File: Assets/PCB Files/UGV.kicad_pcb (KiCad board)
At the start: 2 copper layers, 120.6 x 156.5 mm, 78 parts, among them J13 USB3_A, J15 Screw_Terminal_01x12, J16 Screw_Terminal_01x12, J17 Screw_Terminal_01x12, J18 Screw_Terminal_01x12, Q1 AO3400A, U2 LMR33630ADDA, U3 SN74LVC8T245, U4 Teensy4.1, U5 SN74LVC8T245

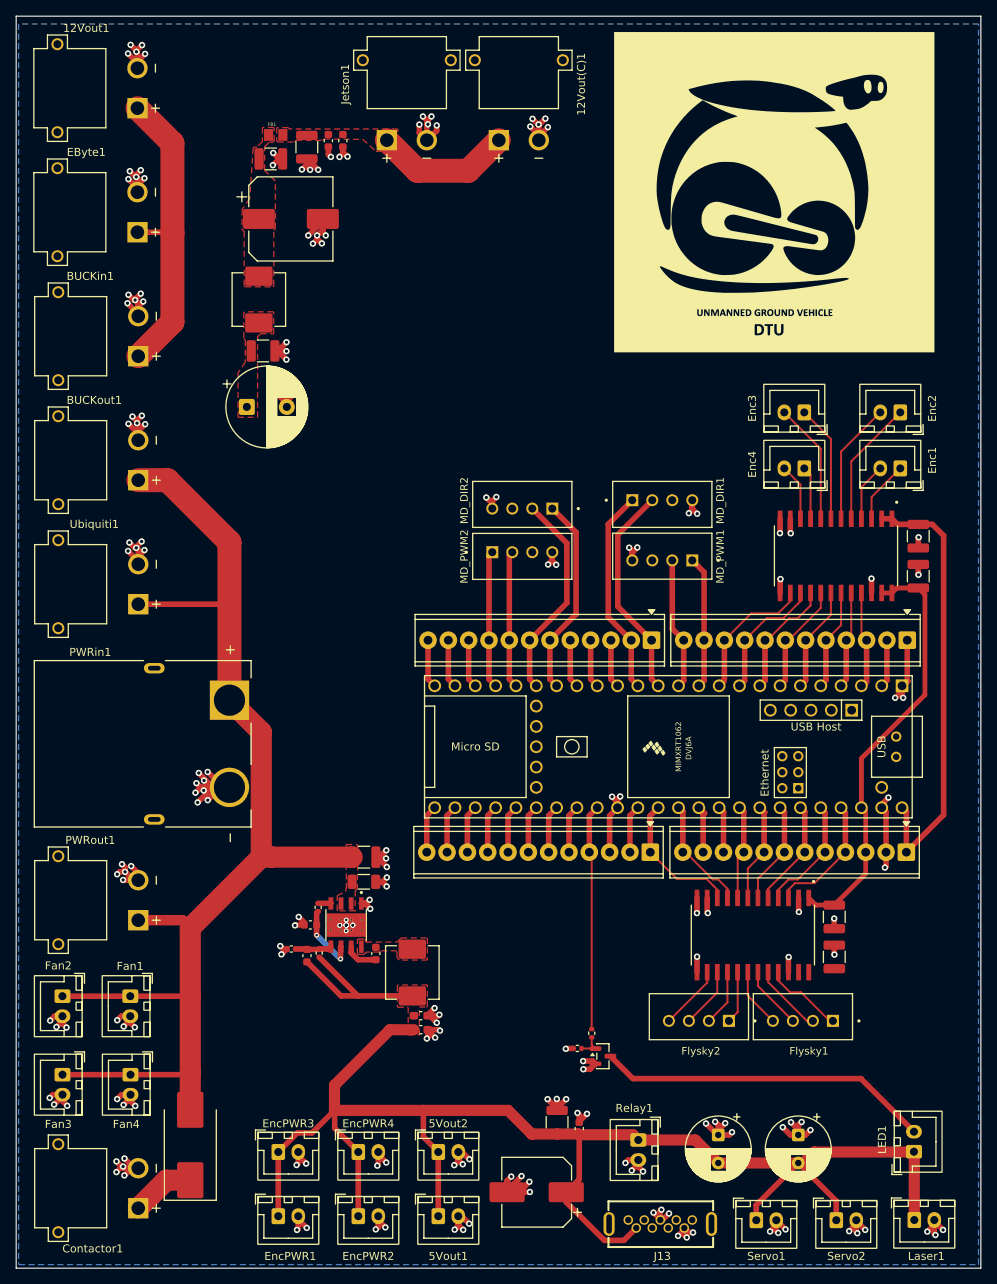
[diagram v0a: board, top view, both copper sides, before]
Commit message: Changed the footprint
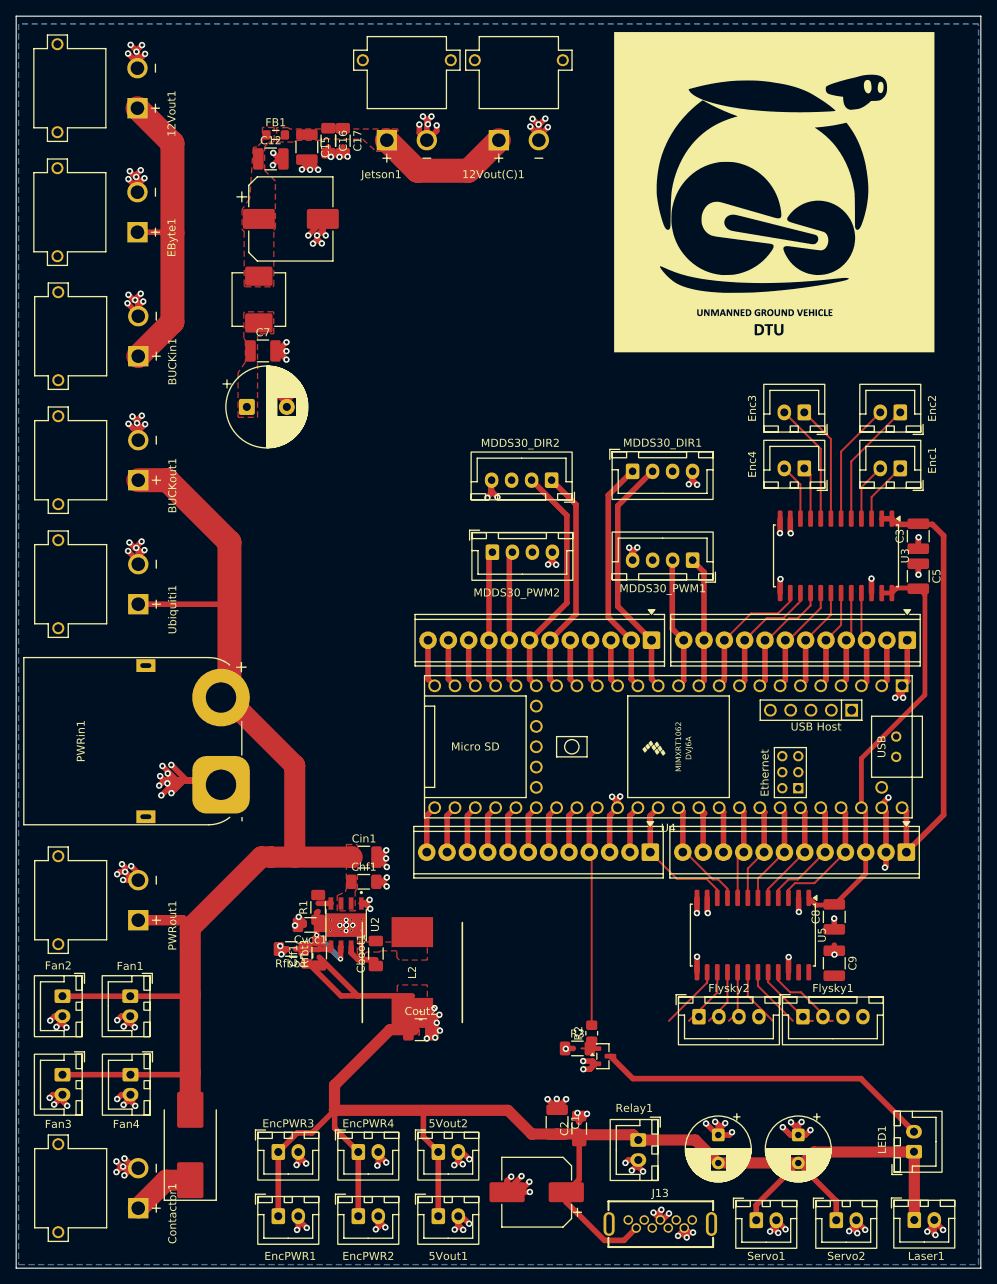
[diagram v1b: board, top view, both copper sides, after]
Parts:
- removed MD_DIR1, MD_DIR2, MD_PWM1, MD_PWM2: B4B-XH-A_LF__SN_, B4B-XH-A_LF__SN_:JST_B4B-XH-A_LF__SN_
- added MDDS30_DIR1: B4B-XH-A_LF__SN_, Connector_JST:JST_XH_B4B-XH-A_1x04_P2.50mm_Vertical, F.Cu at (77.8, 57.9)
- added MDDS30_DIR2: B4B-XH-A_LF__SN_, Connector_JST:JST_XH_B4B-XH-A_1x04_P2.50mm_Vertical, F.Cu at (67.7, 59.0)
- added MDDS30_PWM1: B4B-XH-A_LF__SN_, Connector_JST:JST_XH_B4B-XH-A_1x04_P2.50mm_Vertical, F.Cu at (85.3, 69.0)
- added MDDS30_PWM2: B4B-XH-A_LF__SN_, Connector_JST:JST_XH_B4B-XH-A_1x04_P2.50mm_Vertical, F.Cu at (60.3, 68.0)
- 12Vout(C)1, 12Vout1, BUCKin1, BUCKout1, Contactor1, EByte1, Jetson1, PWRout1, Ubiquiti1: footprint XT30PW-M (1):AMASS_XT30PW-M -> UGV_Custom:AMASS_XT30PW-M
- C1, C12, C15, C3, C5, C7, C8, C9, Cin1: footprint Capacitor_SMD:C_1210_3225Metric -> Capacitor_SMD:C_1210_3225Metric_Pad1.33x2.70mm_HandSolder
- C16, C17, C2, Cboot1, Cvcc1: footprint Capacitor_SMD:C_0603_1608Metric -> Capacitor_SMD:C_1206_3216Metric_Pad1.33x1.80mm_HandSolder
- Cff1: footprint Capacitor_SMD:C_0603_1608Metric -> Capacitor_SMD:C_0805_2012Metric_Pad1.18x1.45mm_HandSolder
- Chf1: footprint Capacitor_SMD:C_1206_3216Metric -> Capacitor_SMD:C_1206_3216Metric_Pad1.33x1.80mm_HandSolder
- Cout2: footprint Capacitor_SMD:C_0603_1608Metric_Pad1.08x0.95mm_HandSolder -> Capacitor_SMD:C_1210_3225Metric_Pad1.33x2.70mm_HandSolder
- Enc1, Enc2, Enc3, Enc4: value B2B-XH-A -> B2B-XH-A-BK
- FB1: footprint BLM21PG220SN1D:BEADC2012X105N -> Inductor_SMD:L_0805_2012Metric_Pad1.05x1.20mm_HandSolder
- Fan1, Fan2, Fan3, Fan4: value B2B-XH-A -> B2B-XH-A-R
- Flysky1, Flysky2: footprint B4B-XH-A_LF__SN_:JST_B4B-XH-A_LF__SN_ -> Connector_JST:JST_XH_B4B-XH-A_1x04_P2.50mm_Vertical
- J13: footprint EasyEDA_Lib:USB-3.0-TH_U233-091N-4BLPC17-11 -> UGV_Custom:USB-3.0-TH_U233-091N-4BLPC17-11
- L2: footprint Inductor_SMD:L_Vishay_IHLP-2525 -> UGV_Custom:SRR1280-101M
- PWRin1: footprint XT90PW-M:AMASS_XT90PW-M -> Connector_AMASS:AMASS_XT90PW-M_1x02_P10.90mm_Horizontal
- R1, Rfbb1, Rfbt1: footprint Resistor_SMD:R_0402_1005Metric -> Resistor_SMD:R_1206_3216Metric_Pad1.30x1.75mm_HandSolder
- R2: footprint Resistor_SMD:R_0402_1005Metric -> Resistor_SMD:R_0805_2012Metric_Pad1.20x1.40mm_HandSolder
- R3: value 10k -> 100k; footprint Resistor_SMD:R_0402_1005Metric -> Resistor_SMD:R_1206_3216Metric_Pad1.30x1.75mm_HandSolder
- U2: footprint LMR33630ADDA:VREG_LM5017MR_NOPB -> UGV_Custom:LMR33630ADDAR
- U3, U5: footprint SN74LVC8T245DWR:SOIC127P1030X265-24N -> Package_SO:SOIC-24W_7.5x15.4mm_P1.27mm
- U4: footprint teensy.pretty-master:Teensy41 -> UGV_Custom:Teensy41
- moved PWRin1 9.79 mm to (26.3, 97.1), turned to 90 degrees
- moved C9 0.79 mm to (103.0, 119.4)
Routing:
- net /11: track 27.1 -> 30.7 mm
- net /12: track 26.0 -> 29.6 mm
- net /27: track 26.2 -> 29.8 mm
- net /26: track 25.1 -> 28.7 mm
- net Net-(D1-A): track 152.7 -> 154.5 mm
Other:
- board text added: "PWRin1"
